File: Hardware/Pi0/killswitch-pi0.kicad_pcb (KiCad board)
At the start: 2 copper layers, 65 x 30 mm, 35 parts, among them J2 REMOTE, J3 PI, Q1 Q_PMOS_GSD, SW1 SW_Push, U1 ATTINY84-20SSU, U2 TSDP341xx, U3 AZ1117-3.3, U4 TXB0108DQSR

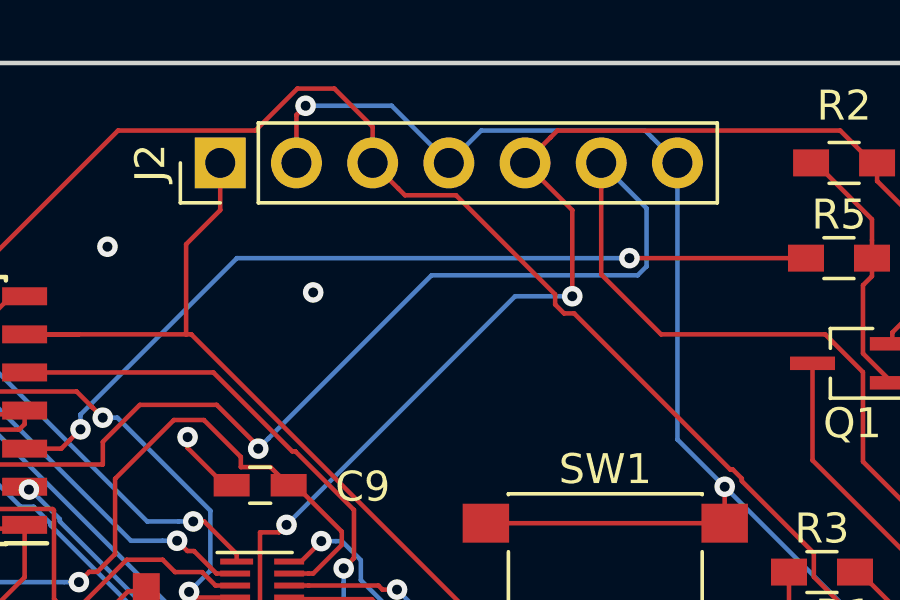
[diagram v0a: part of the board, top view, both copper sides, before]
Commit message: converted make-release to python
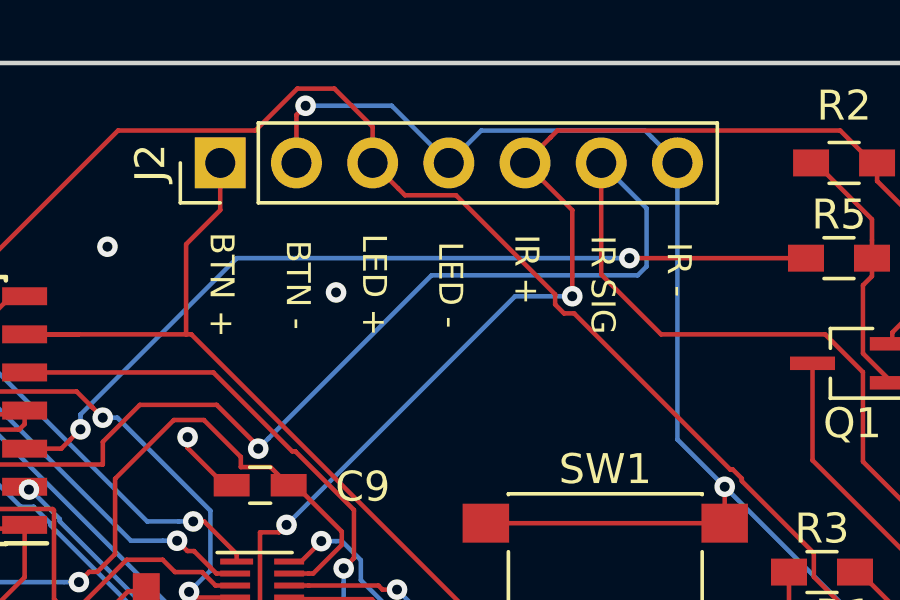
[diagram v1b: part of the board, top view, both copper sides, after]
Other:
- board text added: "BTN +"
- board text added: "BTN -"
- board text added: "IR +"
- board text added: "IR -"
- board text added: "IR SIG"
- board text added: "LED +"
- board text added: "LED -"
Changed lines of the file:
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@@
   (general
     (thickness 1.6)
-    (drawings 13)
+    (drawings 20)
     (tracks 456)
     (zones 0)
@@
   (title_block
     (title "KillSwitch for Pi Zero")
-    (date 2019-03-21)
-    (rev 0.5.2)
+    (date "2019-03-22")
+    (rev "0.5.2-b1")
   )
   (layers
-    (0 F.Cu signal hide)
+    (0 F.Cu signal)
     (31 B.Cu signal hide)
     (32 B.Adhes user)
@@
     (35 F.Paste user)
     (36 B.SilkS user)
-    (37 F.SilkS user hide)
+    (37 F.SilkS user)
     (38 B.Mask user)
     (39 F.Mask user)
@@
     (45 Margin user)
     (46 B.CrtYd user)
-    (47 F.CrtYd user hide)
+    (47 F.CrtYd user)
     (48 B.Fab user)
-    (49 F.Fab user hide)
+    (49 F.Fab user)
   )
   (setup
@@
     (aux_axis_origin 0 0)
     (grid_origin 145 113)
-    (visible_elements FFF9FC9F)
+    (visible_elements FFFDFFFF)
     (pcbplotparams
       (layerselection 0x010fc_ffffffff)
@@
       (xy -2.549664 -1.91989) (xy -2.469928 -1.911165) (xy -2.400256 -1.919918)) (layer B.SilkS) (width 0.01))
   )
+  (gr_text "IR SIG" (at 125.696 90.394 270) (layer F.SilkS)
+    (effects (font (size 0.8 0.8) (thickness 0.1)))
+  )
+  (gr_text "IR -" (at 128.236 89.886 270) (layer F.SilkS)
+    (effects (font (size 0.8 0.8) (thickness 0.1)))
+  )
+  (gr_text "LED +" (at 118.076 90.394 270) (layer F.SilkS)
+    (effects (font (size 0.8 0.8) (thickness 0.1)))
+  )
+  (gr_text "BTN -" (at 115.536 90.394 270) (layer F.SilkS)
+    (effects (font (size 0.8 0.8) (thickness 0.1)))
+  )
+  (gr_text "LED -" (at 120.616 90.394 270) (layer F.SilkS)
+    (effects (font (size 0.8 0.8) (thickness 0.1)))
+  )
+  (gr_text "BTN +" (at 112.996 90.394 270) (layer F.SilkS)
+    (effects (font (size 0.8 0.8) (thickness 0.1)))
+  )
+  (gr_text "IR +" (at 123.156 89.886 270) (layer F.SilkS)
+    (effects (font (size 0.8 0.8) (thickness 0.1)))
+  )
   (gr_text "KillSwitch\nv0.5.2" (at 91.152 99.03 90) (layer B.SilkS)
     (effects (font (size 1.5 1.5) (thickness 0.3)) (justify mirror))
@@
   (segment (start 106.298 98.522) (end 106.425 98.395) (width 0.1524) (layer F.Cu) (net 1))
   (segment (start 103.598 98.522) (end 106.298 98.522) (width 0.1524) (layer F.Cu) (net 1))
-  (via (at 116.044 90.648) (size 0.6858) (drill 0.3302) (layers F.Cu B.Cu) (net 1))
+  (via (at 116.806 90.648) (size 0.6858) (drill 0.3302) (layers F.Cu B.Cu) (net 1))
   (via (at 94.454 103.856) (size 0.6858) (drill 0.3302) (layers F.Cu B.Cu) (net 1))
   (via (at 109.186 89.124) (size 0.6858) (drill 0.3302) (layers F.Cu B.Cu) (net 1))

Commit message: version bump
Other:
- board text added: "KillSwitch v0.5.3-b1"
- board text removed: "KillSwitch v0.5.2"
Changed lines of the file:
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@@
   (title_block
     (title "KillSwitch for Pi Zero")
-    (date "2019-03-22")
-    (rev "0.5.2-b1")
+    (date "2019-03-23")
+    (rev "0.5.3-b1")
   )
   (layers
@@
     (effects (font (size 0.8 0.8) (thickness 0.1)))
   )
-  (gr_text "KillSwitch\nv0.5.2" (at 91.152 99.03 90) (layer B.SilkS)
+  (gr_text "KillSwitch\nv0.5.3-b1" (at 91.152 99.03 90) (layer B.SilkS)
     (effects (font (size 1.5 1.5) (thickness 0.3)) (justify mirror))
   )

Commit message: added error checking to scripts
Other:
- board text added: "KillSwitch v0.5.3-b2"
- board text removed: "KillSwitch v0.5.3-b1"
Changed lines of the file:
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@@
   (title_block
     (title "KillSwitch for Pi Zero")
-    (date "2019-03-23")
-    (rev "0.5.3-b1")
+    (date "2019-03-25")
+    (rev "0.5.3-b2")
   )
   (layers
@@
     (effects (font (size 0.8 0.8) (thickness 0.1)))
   )
-  (gr_text "KillSwitch\nv0.5.3-b1" (at 91.152 99.03 90) (layer B.SilkS)
+  (gr_text "KillSwitch\nv0.5.3-b2" (at 91.152 99.03 90) (layer B.SilkS)
     (effects (font (size 1.5 1.5) (thickness 0.3)) (justify mirror))
   )

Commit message: version bump
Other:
- board text added: "KillSwitch v0.5.4"
- board text removed: "KillSwitch v0.5.3-b2"
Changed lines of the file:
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@@
   (title_block
     (title "KillSwitch for Pi Zero")
-    (date "2019-03-25")
-    (rev "0.5.3-b2")
+    (date "2019-03-27")
+    (rev "0.5.4")
   )
   (layers
@@
     (effects (font (size 0.8 0.8) (thickness 0.1)))
   )
-  (gr_text "KillSwitch\nv0.5.3-b2" (at 91.152 99.03 90) (layer B.SilkS)
+  (gr_text "KillSwitch\nv0.5.4" (at 91.152 99.03 90) (layer B.SilkS)
     (effects (font (size 1.5 1.5) (thickness 0.3)) (justify mirror))
   )

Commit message: version bump
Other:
- board text added: "KillSwitch v0.5.5"
- board text removed: "KillSwitch v0.5.4"
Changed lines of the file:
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@@
   (title_block
     (title "KillSwitch for Pi Zero")
-    (date "2019-03-27")
-    (rev "0.5.4")
+    (date "2019-03-29")
+    (rev "0.5.5")
   )
   (layers
@@
     (effects (font (size 0.8 0.8) (thickness 0.1)))
   )
-  (gr_text "KillSwitch\nv0.5.4" (at 91.152 99.03 90) (layer B.SilkS)
+  (gr_text "KillSwitch\nv0.5.5" (at 91.152 99.03 90) (layer B.SilkS)
     (effects (font (size 1.5 1.5) (thickness 0.3)) (justify mirror))
   )

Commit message: version bump
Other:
- board text added: "KillSwitch v0.5.6"
- board text removed: "KillSwitch v0.5.5"
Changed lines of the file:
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@@
   (title_block
     (title "KillSwitch for Pi Zero")
-    (date "2019-03-29")
-    (rev "0.5.5")
+    (date "2019-03-30")
+    (rev "0.5.6")
   )
   (layers
@@
     (effects (font (size 0.8 0.8) (thickness 0.1)))
   )
-  (gr_text "KillSwitch\nv0.5.5" (at 91.152 99.03 90) (layer B.SilkS)
+  (gr_text "KillSwitch\nv0.5.6" (at 91.152 99.03 90) (layer B.SilkS)
     (effects (font (size 1.5 1.5) (thickness 0.3)) (justify mirror))
   )

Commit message: version bump
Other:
- board text added: "KillSwitch v0.5.7"
- board text removed: "KillSwitch v0.5.6"
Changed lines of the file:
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@@
   (title_block
     (title "KillSwitch for Pi Zero")
-    (date "2019-03-30")
-    (rev "0.5.6")
+    (date "2019-04-02")
+    (rev "0.5.7")
   )
   (layers
@@
     (effects (font (size 0.8 0.8) (thickness 0.1)))
   )
-  (gr_text "KillSwitch\nv0.5.6" (at 91.152 99.03 90) (layer B.SilkS)
+  (gr_text "KillSwitch\nv0.5.7" (at 91.152 99.03 90) (layer B.SilkS)
     (effects (font (size 1.5 1.5) (thickness 0.3)) (justify mirror))
   )

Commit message: version bump
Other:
- board text added: "KillSwitch v0.5.8"
- board text removed: "KillSwitch v0.5.7"
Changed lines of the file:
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@@
     (title "KillSwitch for Pi Zero")
     (date "2019-04-02")
-    (rev "0.5.7")
+    (rev "0.5.8")
   )
   (layers
@@
     (effects (font (size 0.8 0.8) (thickness 0.1)))
   )
-  (gr_text "KillSwitch\nv0.5.7" (at 91.152 99.03 90) (layer B.SilkS)
+  (gr_text "KillSwitch\nv0.5.8" (at 91.152 99.03 90) (layer B.SilkS)
     (effects (font (size 1.5 1.5) (thickness 0.3)) (justify mirror))
   )
